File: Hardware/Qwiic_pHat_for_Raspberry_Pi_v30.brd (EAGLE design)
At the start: 65 x 30.5 mm, 38 parts, among them J1 Qwiic Right Angle, J10 RASPBERRYPI-40-PIN-GPIO_PTH_N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, J8 Qwiic Right Angle

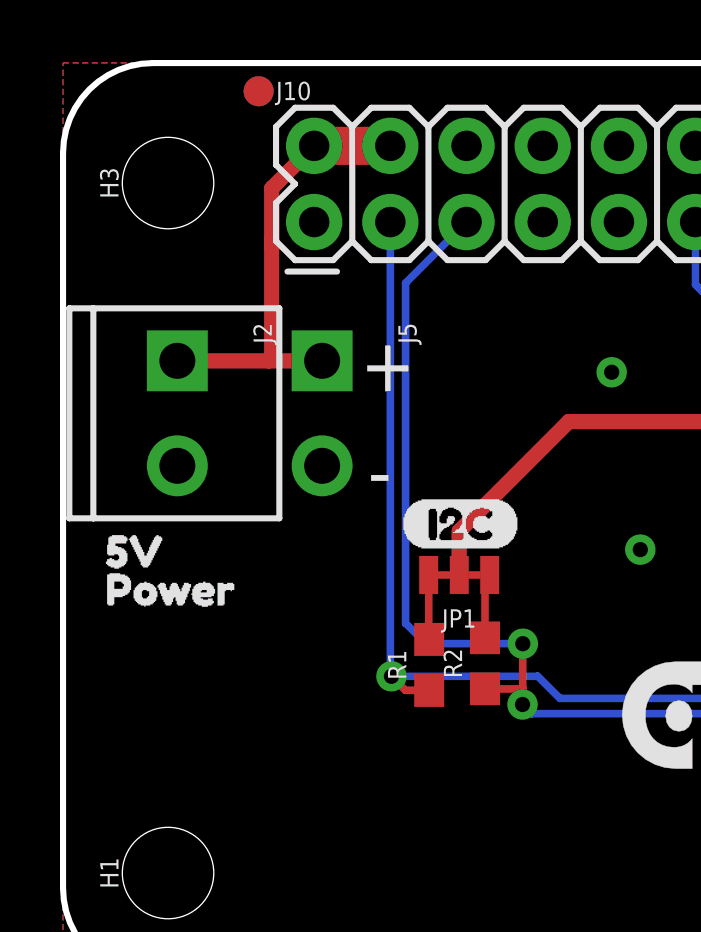
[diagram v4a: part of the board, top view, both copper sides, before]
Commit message: Adds resettable 750mA fuse to 5V power line
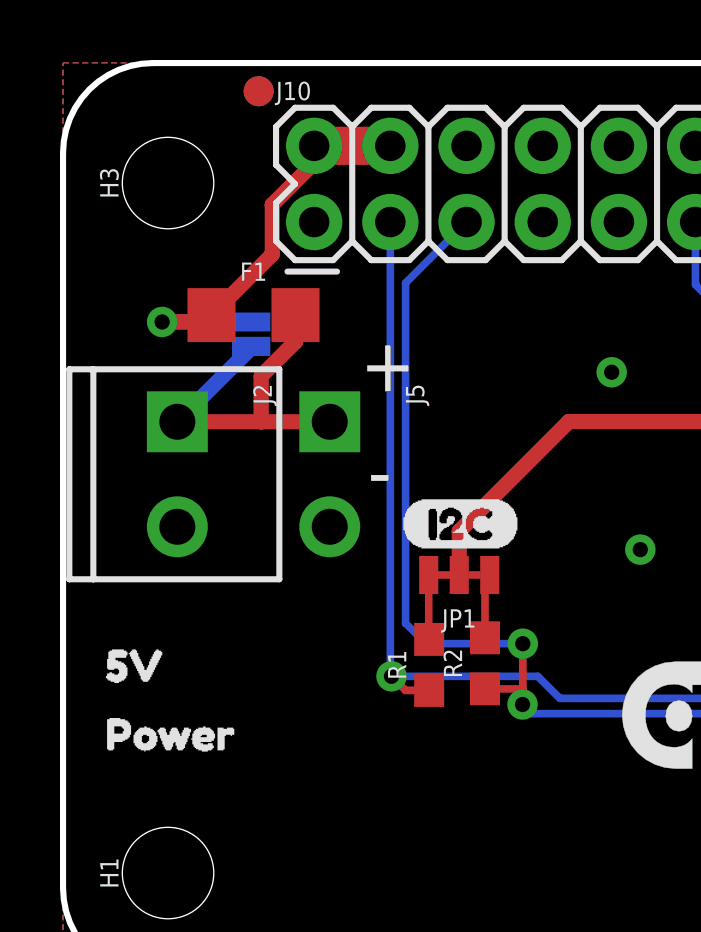
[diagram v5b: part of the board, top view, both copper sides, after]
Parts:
- added F1: 6V/0.75A, SparkFun-Fuses:1206
- added JP2: JUMPER-SMT_2_NO_NO-SILK, SparkFun-Jumpers:SMT-JUMPER_2_NO_NO-SILK
- moved U$11 6.10 mm to (6.60, 8.13)
- moved U$12 5.59 mm to (6.35, 7.37)
- moved U$7 4.83 mm to (0.51, 8.13)
- moved U$6 3.81 mm to (0.51, 10.4)
- moved J5 2.05 mm to (8.89, 18.5)
- moved J2 2.03 mm to (3.81, 18.5)
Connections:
- new net N$2: F1.1, J10.2, J10.4, JP2.1
- net 5V: now also F1.2, JP2.2; no longer J10.2, J10.4
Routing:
- net N$2: track 0.00 -> 14.3 mm, vias 0 -> 1
- net 5V: track 15.2 -> 12.6 mm
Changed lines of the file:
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@@
 <?xml version="1.0" encoding="utf-8"?>
 <!DOCTYPE eagle SYSTEM "eagle.dtd">
-<eagle version="9.4.0">
+<eagle version="9.4.2">
 <drawing>
 <settings>
@@
 <element name="U$4" library="SparkX" package="QWIIC_BOARD_MOUNT_NOHOLES" value="" x="13.6906" y="-6.6802" smashed="yes"/>
 <element name="U$5" library="SparkX" package="QWIIC_BOARD_MOUNT_NOHOLES" value="" x="51.3334" y="-6.6802" smashed="yes"/>
-<element name="J2" library="SparkFun-Connectors" package="SCREWTERMINAL-3.5MM-2" value="" x="3.81" y="20.574" smashed="yes" rot="R270">
-<attribute name="NAME" x="6.35" y="21.844" size="0.6096" layer="25" font="vector" ratio="20" rot="R270"/>
-<attribute name="PROD_ID" value="CONN-08399" x="3.81" y="20.574" size="1.778" layer="27" font="vector" ratio="15" rot="R270" display="off"/>
-<attribute name="VALUE" x="5.08" y="21.844" size="0.6096" layer="27" font="vector" ratio="20" rot="R270"/>
+<element name="J2" library="SparkFun-Connectors" package="SCREWTERMINAL-3.5MM-2" value="" x="3.81" y="18.542" smashed="yes" rot="R270">
+<attribute name="NAME" x="6.35" y="19.812" size="0.6096" layer="25" font="vector" ratio="20" rot="R270"/>
+<attribute name="PROD_ID" value="CONN-08399" x="3.81" y="18.542" size="1.778" layer="27" font="vector" ratio="15" rot="R270" display="off"/>
+<attribute name="VALUE" x="5.08" y="19.812" size="0.6096" layer="27" font="vector" ratio="20" rot="R270"/>
 </element>
 <element name="S1" library="SparkFun-Switches" package="TACTILE_SWITCH_SMD_5.2MM" value="BUTTON GPI017" x="48.768" y="19.558" smashed="yes" rot="R270">
@@
 <attribute name="VALUE" x="35.703" y="10.13366875" size="1.778" layer="27"/>
 </element>
-<element name="J5" library="SparkFun-Connectors" package="SCREWTERMINAL-3.5MM-2-NS" value="" x="8.636" y="20.574" smashed="yes" rot="R270">
-<attribute name="NAME" x="11.176" y="21.844" size="0.6096" layer="25" font="vector" ratio="20" rot="R270"/>
-<attribute name="PROD_ID" value="CONN-08399" x="8.636" y="20.574" size="1.778" layer="27" font="vector" ratio="15" rot="R270" display="off"/>
-<attribute name="VALUE" x="9.906" y="21.844" size="0.6096" layer="27" font="vector" ratio="20" rot="R270"/>
-</element>
-<element name="U$6" library="All labels" package="5V0" value="" x="0.508" y="14.224" smashed="yes"/>
-<element name="U$7" library="All labels" package="POWER1" value="" x="0.508" y="12.954" smashed="yes"/>
+<element name="J5" library="SparkFun-Connectors" package="SCREWTERMINAL-3.5MM-2-NS" value="" x="8.89" y="18.542" smashed="yes" rot="R270">
+<attribute name="NAME" x="11.43" y="19.812" size="0.6096" layer="25" font="vector" ratio="20" rot="R270"/>
+<attribute name="PROD_ID" value="CONN-08399" x="8.89" y="18.542" size="1.778" layer="27" font="vector" ratio="15" rot="R270" display="off"/>
+<attribute name="VALUE" x="10.16" y="19.812" size="0.6096" layer="27" font="vector" ratio="20" rot="R270"/>
+</element>
+<element name="U$6" library="All labels" package="5V0" value="" x="0.508" y="10.414" smashed="yes"/>
+<element name="U$7" library="All labels" package="POWER1" value="" x="0.508" y="8.128" smashed="yes"/>
 <element name="U$8" library="All labels" package="BUTTON2" value="" x="45.466" y="15.24" smashed="yes"/>
 <element name="U$9" library="All labels" package="GPIO173" value="" x="45.466" y="13.716" smashed="yes"/>
 <element name="U$10" library="SparkFun-Aesthetics" package="SFE_LOGO_NAME_FLAME_.3" value="" x="32.258" y="11.684" smashed="yes" rot="MR0"/>
-<element name="U$11" library="All labels" package="5V0" value="" x="6.604" y="14.224" smashed="yes" rot="MR0"/>
-<element name="U$12" library="All labels" package="POWER1" value="" x="6.604" y="12.954" smashed="yes" rot="MR0"/>
+<element name="U$11" library="All labels" package="5V0" value="" x="6.604" y="8.128" smashed="yes" rot="MR0"/>
+<element name="U$12" library="All labels" package="POWER1" value="" x="6.35" y="7.366" smashed="yes" rot="MR0"/>
+<element name="F1" library="SparkFun-Fuses" package="1206" value="6V/0.75A" x="6.35" y="22.098" smashed="yes">
+<attribute name="NAME" x="6.35" y="23.241" size="0.6096" layer="25" font="vector" ratio="20" align="bottom-center"/>
+<attribute name="PROD_ID" value="RES-11150" x="6.35" y="22.098" size="1.778" layer="27" font="vector" ratio="15" display="off"/>
+<attribute name="VALUE" x="6.35" y="20.955" size="0.6096" layer="27" font="vector" ratio="20" align="top-center"/>
+</element>
+<element name="JP2" library="SparkFun-Jumpers" package="SMT-JUMPER_2_NO_NO-SILK" value="JUMPER-SMT_2_NO_NO-SILK" x="6.2738" y="21.463" smashed="yes" rot="MR270">
+<attribute name="NAME" x="5.1308" y="21.463" size="0.6096" layer="26" font="vector" ratio="20" rot="MR270" align="bottom-center"/>
+<attribute name="VALUE" x="7.4168" y="21.463" size="0.6096" layer="28" font="vector" ratio="20" rot="MR270" align="top-center"/>
+</element>
 </elements>
 <signals>
@@
 </signal>
 <signal name="5V">
-<contactref element="J10" pad="2"/>
-<contactref element="J10" pad="4"/>
-<wire x1="8.37" y1="27.74" x2="10.91" y2="27.74" width="1.27" layer="1"/>
 <contactref element="J2" pad="1"/>
-<wire x1="6.9548" y1="24.3788125" x2="6.9548" y2="24.638" width="0.508" layer="1"/>
-<wire x1="6.9548" y1="24.638" x2="6.9548" y2="26.3248" width="0.508" layer="1"/>
-<wire x1="6.9548" y1="26.3248" x2="8.37" y2="27.74" width="0.508" layer="1"/>
 <contactref element="J5" pad="1"/>
-<wire x1="8.636" y1="20.574" x2="6.858" y2="20.574" width="0.508" layer="1"/>
-<wire x1="6.858" y1="20.574" x2="3.81" y2="20.574" width="0.508" layer="1"/>
-<wire x1="6.9548" y1="24.3788125" x2="6.9548" y2="20.6708" width="0.508" layer="1"/>
-<wire x1="6.9548" y1="20.6708" x2="6.858" y2="20.574" width="0.508" layer="1"/>
+<wire x1="8.89" y1="18.542" x2="6.604" y2="18.542" width="0.508" layer="1"/>
+<contactref element="F1" pad="2"/>
+<wire x1="6.604" y1="18.542" x2="3.81" y2="18.542" width="0.508" layer="1"/>
+<wire x1="7.75" y1="22.098" x2="7.75" y2="21.212" width="0.508" layer="1"/>
+<wire x1="7.75" y1="21.212" x2="6.604" y2="20.066" width="0.508" layer="1"/>
+<wire x1="6.604" y1="20.066" x2="6.604" y2="18.542" width="0.508" layer="1"/>
+<contactref element="JP2" pad="2"/>
+<wire x1="6.2738" y1="21.0566" x2="6.2738" y2="21.0058" width="0.508" layer="16"/>
+<wire x1="6.2738" y1="21.0058" x2="3.81" y2="18.542" width="0.508" layer="16"/>
 </signal>
 <signal name="RX">
@@
 <contactref element="J10" pad="1"/>
 </signal>
+<signal name="N$2">
+<contactref element="J10" pad="2"/>
+<contactref element="J10" pad="4"/>
+<wire x1="8.37" y1="27.74" x2="10.91" y2="27.74" width="1.27" layer="1"/>
+<wire x1="8.37" y1="27.1756625" x2="8.37" y2="27.74" width="0.508" layer="1"/>
+<wire x1="6.973" y1="24.121" x2="6.973" y2="25.7786625" width="0.508" layer="1"/>
+<wire x1="6.973" y1="25.7786625" x2="8.37" y2="27.1756625" width="0.508" layer="1"/>
+<contactref element="F1" pad="1"/>
+<contactref element="JP2" pad="1"/>
+<wire x1="4.95" y1="22.098" x2="6.973" y2="24.121" width="0.508" layer="1"/>
+<wire x1="6.2738" y1="21.8694" x2="3.302" y2="21.8694" width="0.508" layer="16"/>
+<via x="3.302" y="21.8694" extent="1-16" drill="0.508"/>
+<wire x1="4.7214" y1="21.8694" x2="4.95" y2="22.098" width="0.508" layer="1"/>
+<wire x1="4.7214" y1="21.8694" x2="3.302" y2="21.8694" width="0.508" layer="1"/>
+</signal>
 </signals>

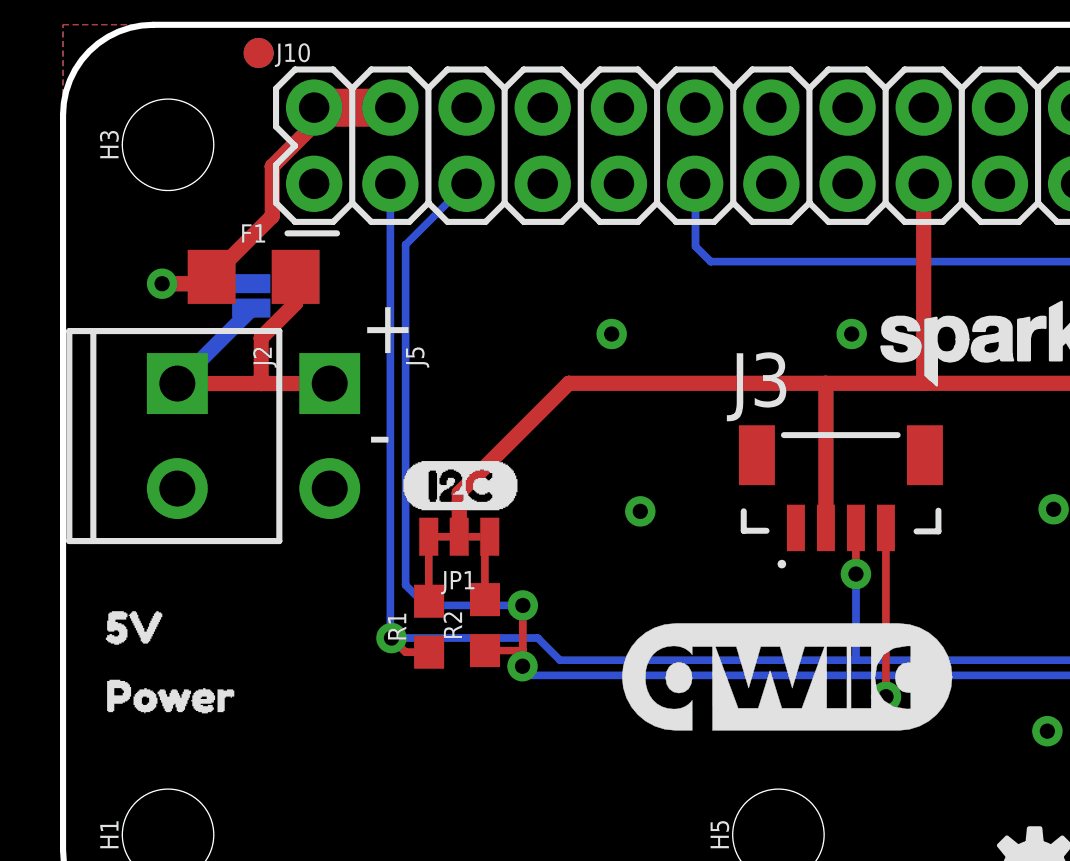
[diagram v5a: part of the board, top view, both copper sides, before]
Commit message: Moves 5V screw terminal and pull up resistors away from each other
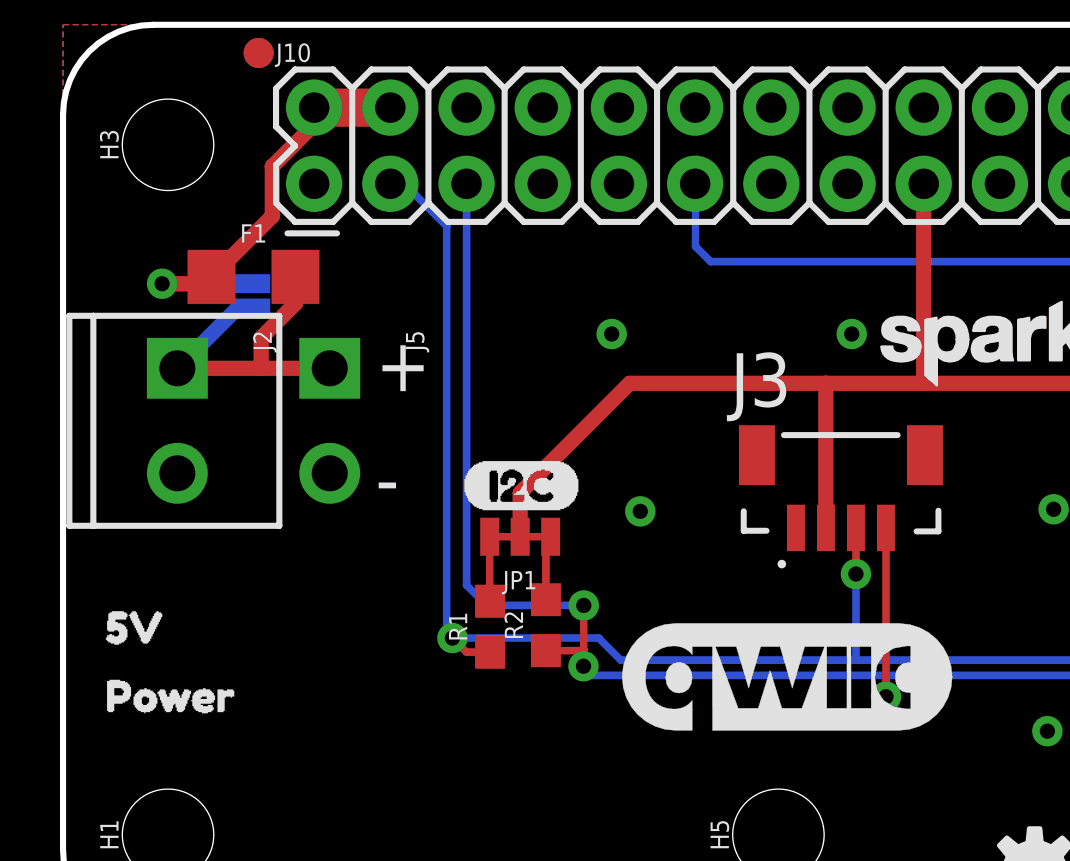
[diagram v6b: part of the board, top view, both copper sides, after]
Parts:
- moved JP1 2.03 mm to (15.2, 13.4)
- moved R1 2.03 mm to (14.2, 10.4)
- moved R2 2.03 mm to (16.1, 10.5)
- moved U$2 2.03 mm to (13.3, 15.1)
- moved J2 0.51 mm to (3.81, 19.1)
- moved J5 0.51 mm to (8.89, 19.1)
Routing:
- net SCL: track 96.6 -> 93.8 mm
- net 3.3V: track 78.7 -> 76.6 mm
- net SDA: track 88.3 -> 87.4 mm
- net 5V: track 12.6 -> 11.9 mm

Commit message: Updates the silk
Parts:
- removed J10: RASPBERRYPI-40-PIN-GPIO_PTH_NO_SHROUD, SparkFun-Connectors:2X20
- added J6: (no value), SparkFun-Connectors:JST04_1MM_VERT
- added U$13, U$14: (no value), POWER:POWER1
- added U$15: (no value), POWER:5V0
- added U$16: (no value), SparkFun-Aesthetics:QWIIC_3MM
- J1: value Qwiic Right Angle -> RASPBERRYPI-40-PIN-GPIO_PTH_NO_SHROUD; device SparkFun-Connectors:JST04_1MM_RA -> SparkFun-Connectors:2X20
- J2: device SparkFun-Connectors:SCREWTERMINAL-3.5MM-2 -> SparkFun-Connectors:SCREWTERMINAL-3.5MM-2-NS
- J3: device SparkFun-Connectors:JST04_1MM_VERT -> SparkFun-Connectors:SCREWTERMINAL-3.5MM-2
- J4: value (none) -> Qwiic Right Angle; device SparkFun-Connectors:JST04_1MM_VERT -> SparkFun-Connectors:JST04_1MM_RA
- J5: device SparkFun-Connectors:SCREWTERMINAL-3.5MM-2-NS -> SparkFun-Connectors:JST04_1MM_VERT
- JP1: value PULLUP -> JUMPER-SMT_2_NO_SILK; device SparkFun-Jumpers:SMT-JUMPER_3_2-NC_TRACE_NO-SILK -> SparkFun-Jumpers:SMT-JUMPER_2_NO_SILK
- JP2: value JUMPER-SMT_2_NO_NO-SILK -> PULLUP; device SparkFun-Jumpers:SMT-JUMPER_2_NO_NO-SILK -> SparkFun-Jumpers:SMT-JUMPER_3_2-NC_TRACE_NO-SILK
- LOGO1: value SFE_LOGO_NAME_FLAME.1_INCH -> REVISION; device SparkFun-Aesthetics:SFE_LOGO_NAME_FLAME_.1 -> SparkFun-Aesthetics:REVISION
- LOGO2: value REVISION -> OSHW-LOGOS; device SparkFun-Aesthetics:REVISION -> SparkFun-Aesthetics:OSHW-LOGO-S
- LOGO3: value OSHW-LOGOS -> SFE_LOGO_NAME_FLAME.1_INCH; device SparkFun-Aesthetics:OSHW-LOGO-S -> SparkFun-Aesthetics:SFE_LOGO_NAME_FLAME_.1
- U$1: device SparkFun-Aesthetics:QWIIC_11MM -> Qwiic:QWIIC1
- U$11: device All labels:5V0 -> SparkFun-Aesthetics:QWIIC_3MM
- U$12: device All labels:POWER1 -> POWER:5V0
- U$6: device All labels:5V0 -> Fuse Bypass:FUSE0
- U$7: device All labels:POWER1 -> Fuse Bypass:BYPASS1
- moved H1 62.4 mm to (61.5, 26.5)
- moved LOGO1 58.5 mm to (4.32, -31.2)
- moved U$11 58.4 mm to (63.0, 23.4), flipped to the top
- moved H4 58.0 mm to (3.50, 26.5)
- moved J1 53.4 mm to (8.37, 25.2), turned to 0 degrees
- moved LOGO2 43.7 mm to (32.4, 2.22)
- moved H3 30.7 mm to (23.8, 3.50)
- moved J4 22.2 mm to (59.7, 10.4), turned to 90 degrees
- moved J3 21.2 mm to (3.81, 19.1), turned to 270 degrees
- moved U$7 20.4 mm to (16.3, 21.1), flipped to the bottom
- moved H5 20.3 mm to (3.50, 3.50)
- moved H2 20.3 mm to (41.2, 3.50)
- moved H6 20.3 mm to (61.5, 3.50)
- moved U$6 18.4 mm to (14.2, 22.6), flipped to the bottom
- moved LOGO3 17.7 mm to (32.8, 19.9)
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- renumbered J8 to J7
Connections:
- net 3.3V: now also J1.17, J5.2, J6.2, JP2.2; no longer J1.2, J10.17, J3.2, JP1.2
- net 5V: now also J3.1, JP1.2; no longer J5.1, JP2.2
- net BUTTON/D17: now also J1.11; no longer J10.11
- net D12: now also J1.32; no longer J10.32
- net D13: now also J1.33; no longer J10.33
- net D16: now also J1.36; no longer J10.36
- net D18: now also J1.12; no longer J10.12
- net D19: now also J1.35; no longer J10.35
- net D20: now also J1.38; no longer J10.38
- net D21: now also J1.40; no longer J10.40
- net D22: now also J1.15; no longer J10.15
- net D23: now also J1.16; no longer J10.16
- net D24: now also J1.18; no longer J10.18
- net D25: now also J1.22; no longer J10.22
- net D26: now also J1.37; no longer J10.37
- net D27: now also J1.13; no longer J10.13
- net D4: now also J1.7; no longer J10.7
- net D5: now also J1.29; no longer J10.29
- net D6: now also J1.31; no longer J10.31
- net GND: now also J1.14, J1.20, J1.25, J1.30, J1.34, J1.39, J1.6, J1.9, J3.2, J5.1, J6.1; no longer J1.1, J10.14, J10.20, J10.25, J10.30, J10.34, J10.39, J10.6, J10.9, J3.1, J5.2
- net ID_SCL: now also J1.28; no longer J10.28
- net ID_SDA: now also J1.27; no longer J10.27
- net MISO: now also J1.21; no longer J10.21
- net MOSI: now also J1.19; no longer J10.19
- net N$1: now also J1.1; no longer J10.1
- net N$2: now also J1.2, J1.4, JP1.1; no longer J10.2, J10.4, JP2.1
- net N$3: now also JP2.3; no longer JP1.3
- net N$4: now also JP2.1; no longer JP1.1
- net RX: now also J1.10; no longer J10.10
- net SCK: now also J1.23; no longer J10.23
- net SCL: now also J1.5, J5.4, J6.4; no longer J1.4, J10.5, J3.4
- net SDA: now also J5.3, J6.3; no longer J10.3, J3.3
- net TX: now also J1.8; no longer J10.8
